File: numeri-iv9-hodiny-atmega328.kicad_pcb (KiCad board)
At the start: 2 copper layers, 160 x 50 mm, 77 parts, among them J2 Screw_Terminal_01x04, J4 PINHD_1x3_Female, J5 HW-084, J6 2x3, J7 1x2, SW1 RESET, U1 ATmega328-P, U2 TPIC6B595N, U3 TPIC6B595N, U4 TPIC6B595N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

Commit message: Nové fotky a úpravy stránky.
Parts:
- TLACIDLO1: value Horizontal -> Control
- TLACIDLO2: value Vertical -> Control
- U1: value ATmega328-P -> ATmega328/ATmega328P
- U2, U3, U4, U5: value TPIC6B595N -> TPIC6B595N/TPIC6595N
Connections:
- net DEC_ENA renamed LDR
- U1 pad 25: DEC_OUT -> unconnected-(U1-PC2-Pad25)
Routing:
- net unconnected-(U1-PC2-Pad25): track 0.00 -> 3.97 mm, vias 0 -> 1
- net DEC_OUT: track 3.97 -> 0.00 mm, vias 1 -> 0

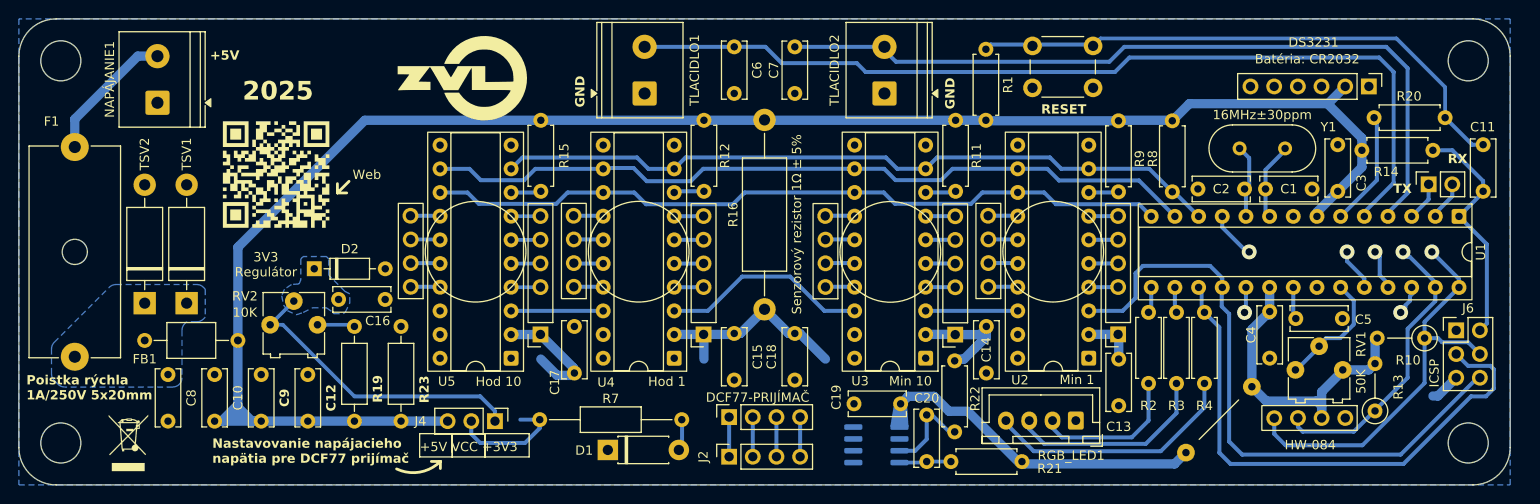
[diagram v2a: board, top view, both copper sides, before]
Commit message: Dalsie masivne zmeny. Pridané casovace, aj ked zatial este moc nefunguju.
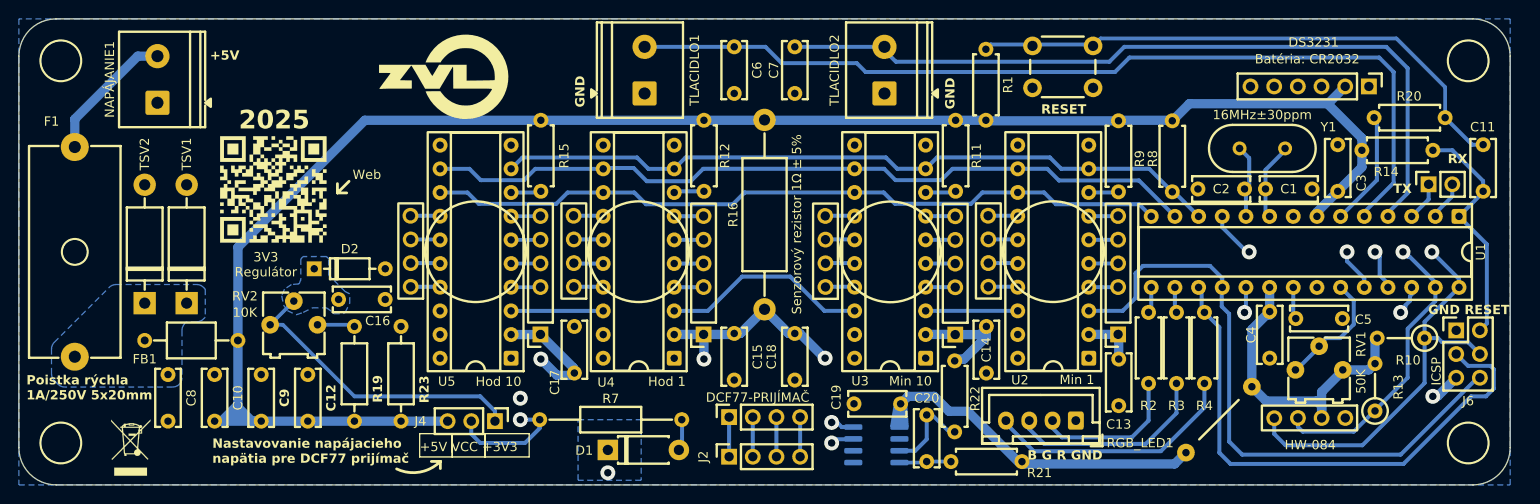
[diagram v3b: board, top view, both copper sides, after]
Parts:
- removed the G*** at (111.6, 76.8)
- removed the G*** at (91.6, 87.2)
- added G***: LOGO, LOGO, F.Cu at (109.6, 76.7)
- added G***: LOGO, LOGO, F.Cu at (91.3, 88.8)
- added REF**: LED, PanelMount:LED, F.Cu at (166.5, 75.0)
- added REF**: Switch, PanelMount:Switch, F.Cu at (121.5, 75.0)
- added REF**: Button, PanelMount:Button, F.Cu at (185.5, 75.0)
- added REF**: Button, PanelMount:Button, F.Cu at (102.5, 75.0)
- added REF**: DCF77_ANTENNA_140x10mm, PanelMount:DCF77_ANTENNA_140x10mm, F.Cu at (144.5, 120.5)
- TLACIDLO1: value Control -> Horizontal
- TLACIDLO2: value Control -> Vertical
- U1: value ATmega328/ATmega328P -> ATmega328-P
- U2, U3, U4, U5: value TPIC6B595N/TPIC6595N -> TPIC6B595N
- moved REF** 0.56 mm to (76.0, 116.5)
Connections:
- net LDR renamed DEC_ENA
- U1 pad 25: unconnected-(U1-PC2-Pad25) -> DEC_OUT
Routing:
- net unconnected-(U1-PC2-Pad25): track 3.97 -> 0.00 mm, vias 1 -> 0
- net DEC_OUT: track 0.00 -> 3.97 mm, vias 0 -> 1
- net SCL: track 44.5 -> 47.3 mm, vias 1 -> 2
- net SDA: track 31.1 -> 33.5 mm, vias 1 -> 2
- net PB5: vias 1 -> 2
- net GND: vias 0 -> 1
- net +5V/+3V3: vias 0 -> 1
- net +5V_ICSP: vias 0 -> 1
- net +5V_DEC: vias 0 -> 3
- added copper zone on B.Cu, net PB5
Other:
- board text added: "B G R GND"
- board text added: "GND RESET"

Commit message: Upravený návrh dosky.
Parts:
- removed the REF** at (76.0, 116.5)
- added R18: 620R, Resistor_THT:R_Axial_DIN0207_L6.3mm_D2.5mm_P7.62mm_Horizontal, F.Cu at (182.2, 76.5)
- added R25: 620R, Resistor_THT:R_Axial_DIN0207_L6.3mm_D2.5mm_P7.62mm_Horizontal, F.Cu at (184.5, 74.0)
- C1, C2: value 68pF±5% -> 33pF±5%
- R16: value 1R±5% -> 0R33
- TLACIDLO1: value Horizontal -> Control
- TLACIDLO2: value Vertical -> Control
- U1: value ATmega328-P -> ATmega328/ATmega328P
- U2, U3, U4, U5: value TPIC6B595N -> TPIC6B595N/TPIC6595N
- moved REF** 0.71 mm to (220.0, 116.5)
- moved REF** 0.71 mm to (220.0, 74.5)
- moved REF** 0.71 mm to (68.0, 116.5)
- moved REF** 0.71 mm to (68.0, 74.5)
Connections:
- net DEC_ENA renamed LDR
- net PD4 renamed RSTBTN
- C6 pad 2: HBTN -> Net-(C6-Pad2)
- C7 pad 2: VBTN -> Net-(C7-Pad2)
- D1 pad 1: PB5 -> SCK/~{PON}
- J6 pad 4: SCL -> SCK/~{PON}
- TLACIDLO1 pad 2: HBTN -> Net-(C6-Pad2)
- TLACIDLO2 pad 2: VBTN -> Net-(C7-Pad2)
- U1 pad 19: PB5 -> SCK/~{PON}
- U1 pad 25: DEC_OUT -> unconnected-(U1-PC2-Pad25)
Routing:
- net SCK/~{PON}: track 0.00 -> 115.4 mm, vias 0 -> 2
- net HBTN: track 98.1 -> 39.4 mm
- net SDA: track 33.5 -> 87.6 mm
- net Net-(C6-Pad2): track 0.00 -> 52.3 mm
- net VBTN: track 84.2 -> 38.4 mm
- net SCL: track 47.3 -> 90.2 mm
- net Net-(C7-Pad2): track 0.00 -> 38.1 mm
- net unconnected-(U1-PC2-Pad25): track 0.00 -> 3.97 mm, vias 0 -> 1
- net DEC_OUT: track 3.97 -> 0.00 mm, vias 1 -> 0
- net PB5: track 2.75 -> 0.00 mm, vias 2 -> 0
- added copper zone on B.Cu, net SCK/~{PON}
- removed copper zone on B.Cu, net PB5
